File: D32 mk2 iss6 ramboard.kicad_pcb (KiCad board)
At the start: 2 copper layers, 117.5 x 53.3 mm, 35 parts, among them IC1 4116, IC2 4116, IC3 4116, IC36 4116, IC37 4116, IC38 4116, IC39 4116, IC4 4116, IC40 4116, IC41 4116, IC42 4116, IC43 4116, IC5 4116, IC6 4116, IC7 4116, IC8 4116, U1 4164, U10 4164, U11 4164, U12 4164, U13 4164, U14 4164, U15 4164, U16 4164, U2 4164, U3 4164, U4 4164, U5 4164, U6 4164, U7 4164, U8 4164, U9 4164

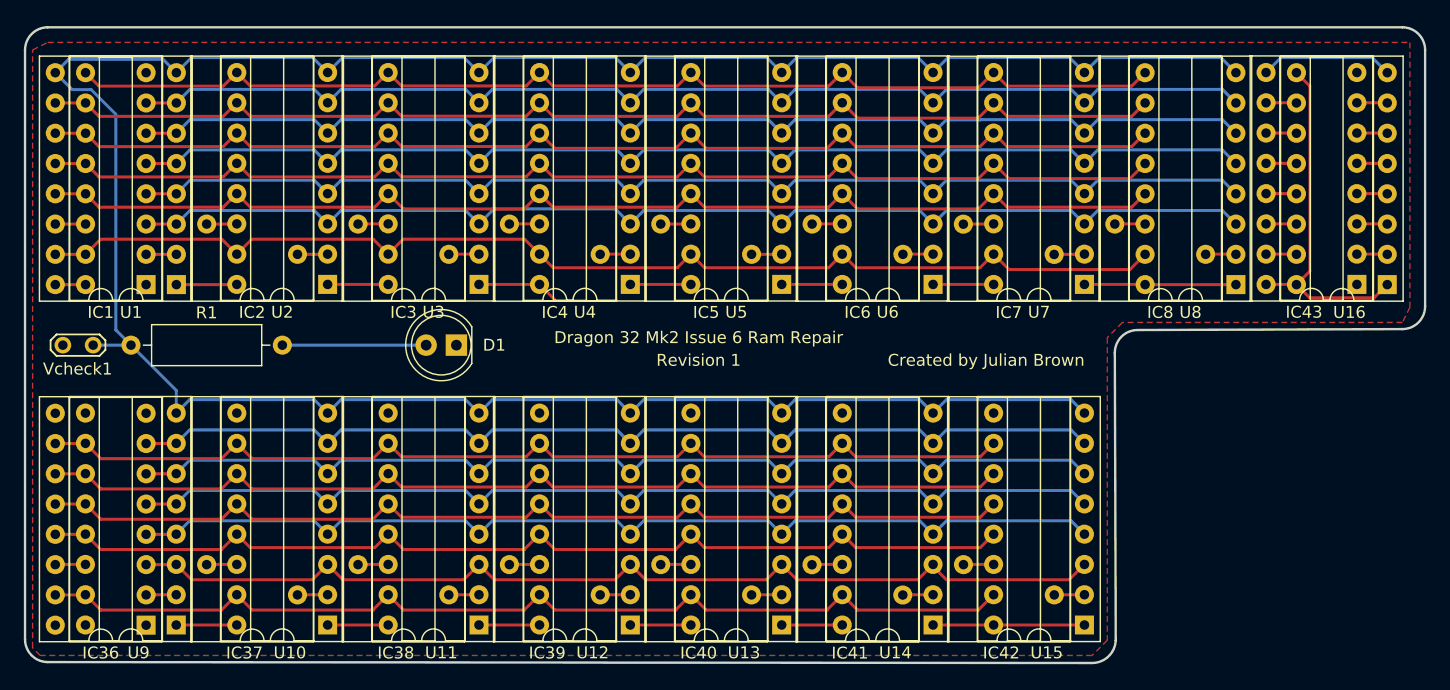
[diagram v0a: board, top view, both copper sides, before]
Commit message: make A8 configurable on each bank
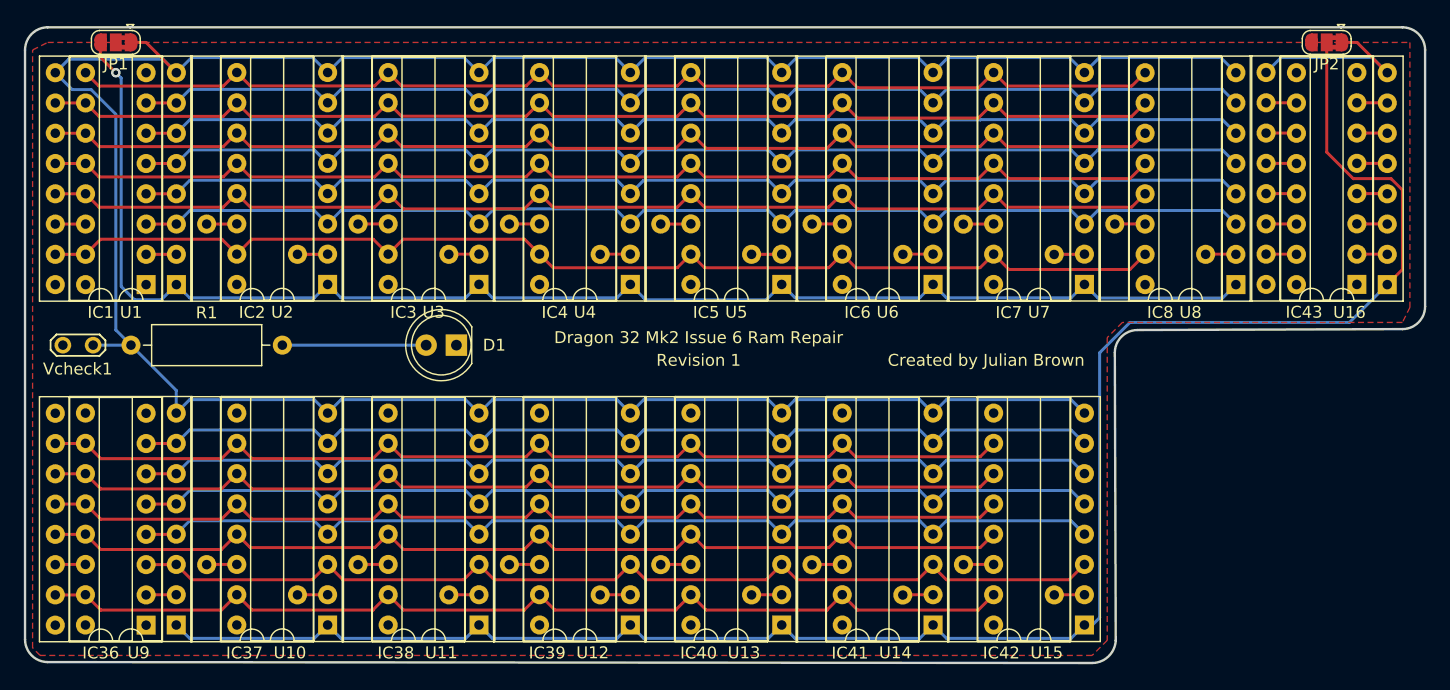
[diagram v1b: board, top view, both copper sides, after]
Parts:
- added JP1: A8_jumper, Jumper:SolderJumper-3_P1.3mm_Bridged2Bar12_RoundedPad1.0x1.5mm, F.Cu at (94.0, 66.0)
- added JP2: A8_jumper, Jumper:SolderJumper-3_P1.3mm_Bridged2Bar12_RoundedPad1.0x1.5mm, F.Cu at (195.6, 66.0)
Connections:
- IC43 pad 16: Net-(IC43-Pad16) -> GND
- U1 pad 1: GND -> Net-(U1-Pad1)
- U10 pad 1: GND -> Net-(U16-Pad1)
- U11 pad 1: GND -> Net-(U16-Pad1)
- U12 pad 1: GND -> Net-(U16-Pad1)
- U13 pad 1: GND -> Net-(U16-Pad1)
- U14 pad 1: GND -> Net-(U16-Pad1)
- U15 pad 1: GND -> Net-(U16-Pad1)
- U16 pad 1: Net-(IC43-Pad16) -> Net-(U16-Pad1)
- U16 pad 16: Net-(IC43-Pad16) -> GND
- U16 pad 9: Net-(IC43-Pad16) -> GND
- U2 pad 1: GND -> Net-(U1-Pad1)
- U3 pad 1: GND -> Net-(U1-Pad1)
- U4 pad 1: GND -> Net-(U1-Pad1)
- U5 pad 1: GND -> Net-(U1-Pad1)
- U6 pad 1: GND -> Net-(U1-Pad1)
- U7 pad 1: GND -> Net-(U1-Pad1)
- U8 pad 1: GND -> Net-(U1-Pad1)
- U9 pad 1: GND -> Net-(U16-Pad1)
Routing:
- net Net-(U16-Pad1): track 0.00 -> 156.9 mm
- net Net-(U1-Pad1): track 0.00 -> 122.4 mm, vias 0 -> 1
- net GND: track 181.2 -> 95.6 mm
- net Net-(IC43-Pad16): track 29.8 -> 0.00 mm
- net +5V: track 225.9 -> 230.8 mm
- net Net-(IC43-Pad9): track 11.2 -> 16.0 mm
